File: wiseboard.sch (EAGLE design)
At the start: 87 parts, among them CN1 455-1749-1-ND, CN3 455-1749-1-ND, IC1 MCP73871-2CCI/ML-ND, IC2 LM358MX, Q1 IRLML6402TRPBF, Q2 IRLML6402TRPBF, U1 LT1945EMSPBF, X1 1528-1438-ND

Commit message: ADD ESP DEBUG HEADERS AND ROUGH AUTOROUTE
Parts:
- added ESPDEBUG_1, ESPDEBUG_2: (no value), pinhead:PINHD-1X8
- added INPUTBUTTONHEADER: (no value), pinhead:PINHD-1X2
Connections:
- removed net GPIO2: R24.1
- removed net N$12: JP3.1, X1.GPIO16
- removed net N$17: C8.1, CN1.1, IC1.VBAT1, IC1.VBAT2, IC1.VBAT3, JP2.1
- new net +3V1: ESPDEBUG_1.8
- new net GND1: ESPDEBUG_2.8
- new net GPIO16: ESPDEBUG_1.4, JP3.1, X1.GPIO16
- net +3V3: now also INPUTBUTTONHEADER.1
- net ADC: now also ESPDEBUG_1.2
- net BOOSTENA: now also ESPDEBUG_2.6, R24.1
- net CH_PD: now also ESPDEBUG_1.3
- net CL: now also ESPDEBUG_2.4
- net GPIO0: now also ESPDEBUG_2.5
- net GPIO12: now also ESPDEBUG_1.6; no longer U$13.S
- net GPIO13: now also ESPDEBUG_1.7
- net GPIO14: now also ESPDEBUG_1.5
- net GPIO15: now also ESPDEBUG_2.7
- net N$25: now also U$14.VIN
- net N$26: now also INPUTBUTTONHEADER.2
- net OE: now also ESPDEBUG_2.3
- net RESET: now also ESPDEBUG_1.1
- net RXD: now also ESPDEBUG_2.2, U$13.S
- net TXD: now also ESPDEBUG_2.1
- net VBAT: now also C8.1, CN1.1, IC1.VBAT1, IC1.VBAT2, IC1.VBAT3, JP2.1; no longer U$14.VIN
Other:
- note added: "ESP DEBUG HEADER"
- moved on the sheet: D2

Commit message: PASS ERC SCHEMATIC TEST AND ADD SUPPLY SYMBOLS
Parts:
- removed C13: 1uF, adafruit:C-USC1206
- added INPUTBUTTONHEADER1, SOLARPIN: (no value), pinhead:PINHD-1X2
- C2: value (none) -> 2u2F
- C4: value (none) -> 100pF
- renumbered CN3 to SOLAR
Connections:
- net +20V renamed -20V
- removed net +24V: U$4.GVDD
- removed net +3V1: ESPDEBUG_1.8
- removed net GND1: ESPDEBUG_2.8
- new net +22V: C5.1, R6.2, U$2.VIN, U$4.GVDD, U$8.C
- net +3V3: now also ESPDEBUG_1.8, INPUTBUTTONHEADER1.1
- net ADC: no longer C13.1, U$13.GND
- net GND: now also ESPDEBUG_2.8, SOLARPIN.1, U$13.GND; no longer C13.2
- net GPIO16: now also JP3.2; no longer JP3.1
- net N$26: now also INPUTBUTTONHEADER1.2
- net N$7: now also SOLARPIN.2
- net RESET: now also JP3.1; no longer JP3.2
- net VCC: no longer C5.1, R6.2, U$2.VIN, U$8.C
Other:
- moved on the sheet: JP3

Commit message: RESOLVE CONSISTENCY ISSUES, IGNORE
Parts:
- CN1: value 455-1749-1-ND -> (none)
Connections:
- net GND: now also CN1.1; no longer CN1.2
- net VBAT: now also CN1.2; no longer CN1.1
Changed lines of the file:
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@@
 <layer number="19" name="Unrouted" color="6" fill="1" visible="no" active="no"/>
 <layer number="20" name="Dimension" color="15" fill="1" visible="no" active="no"/>
-<layer number="21" name="tPlace" color="14" fill="1" visible="no" active="no"/>
+<layer number="21" name="tPlace" color="7" fill="1" visible="no" active="no"/>
 <layer number="22" name="bPlace" color="7" fill="1" visible="no" active="no"/>
 <layer number="23" name="tOrigins" color="15" fill="1" visible="no" active="no"/>
@@
 <part name="U$2" library="WISE" deviceset="L78L15" device="" value="497-7278-1-ND"/>
 <part name="U$3" library="WISE" deviceset="L79L15" device="" value="497-7303-1-ND"/>
-<part name="CN1" library="adafruit" deviceset="JST_2PIN" device="-SMT-RA" value="455-1749-1-ND"/>
 <part name="C1" library="adafruit" deviceset="C-US" device="C1206" value="100nF"/>
 <part name="22" library="WISE" deviceset="587-2103-1-ND" device=""/>
@@
 <part name="GND14" library="supply1" library_urn="urn:adsk.eagle:library:371" deviceset="GND" device=""/>
 <part name="GND15" library="supply1" library_urn="urn:adsk.eagle:library:371" deviceset="GND" device=""/>
-<part name="GND16" library="supply1" library_urn="urn:adsk.eagle:library:371" deviceset="GND" device=""/>
 <part name="C8" library="adafruit" deviceset="C-US" device="C1206" value="10uF"/>
 <part name="GND17" library="supply1" library_urn="urn:adsk.eagle:library:371" deviceset="GND" device=""/>
@@
 <part name="U$19" library="WISE" deviceset="-15V" device=""/>
 <part name="GND46" library="supply1" library_urn="urn:adsk.eagle:library:371" deviceset="GND" device=""/>
+<part name="CN1" library="adafruit" deviceset="JST_2PIN" device="-SMT-RA"/>
+<part name="GND16" library="supply1" library_urn="urn:adsk.eagle:library:371" deviceset="GND" device=""/>
 </parts>
 <sheets>
@@
 <instance part="U$2" gate="G$1" x="-144.78" y="-78.74"/>
 <instance part="U$3" gate="G$1" x="-144.78" y="-7.62"/>
-<instance part="CN1" gate="G$1" x="375.92" y="-154.94"/>
 <instance part="C1" gate="G$1" x="-114.3" y="-7.62"/>
 <instance part="22" gate="G$1" x="-261.62" y="-5.08" rot="R90"/>
@@
 <instance part="GND14" gate="1" x="-124.46" y="-20.32" rot="R90"/>
 <instance part="GND15" gate="1" x="304.8" y="-177.8"/>
-<instance part="GND16" gate="1" x="358.14" y="-157.48"/>
 <instance part="C8" gate="G$1" x="353.06" y="-165.1"/>
 <instance part="GND17" gate="1" x="353.06" y="-175.26"/>
@@
 <instance part="U$19" gate="G$1" x="-124.46" y="60.96"/>
 <instance part="GND46" gate="1" x="-363.22" y="58.42" rot="R270"/>
+<instance part="CN1" gate="G$1" x="375.92" y="-154.94"/>
+<instance part="GND16" gate="1" x="360.68" y="-152.4" rot="R270"/>
 </instances>
 <busses>
@@
 </segment>
 <segment>
-<pinref part="CN1" gate="G$1" pin="2"/>
-<pinref part="GND16" gate="1" pin="GND"/>
-<wire x1="373.38" y1="-154.94" x2="358.14" y2="-154.94" width="0.1524" layer="91"/>
-</segment>
-<segment>
 <pinref part="C8" gate="G$1" pin="2"/>
 <pinref part="GND17" gate="1" pin="GND"/>
@@
 <wire x1="-360.68" y1="58.42" x2="-342.9" y2="58.42" width="0.1524" layer="91"/>
 <pinref part="GND46" gate="1" pin="GND"/>
+</segment>
+<segment>
+<pinref part="CN1" gate="G$1" pin="1"/>
+<wire x1="373.38" y1="-152.4" x2="363.22" y2="-152.4" width="0.1524" layer="91"/>
+<pinref part="GND16" gate="1" pin="GND"/>
 </segment>
 </net>
@@
 <junction x="327.66" y="-149.86"/>
 <junction x="327.66" y="-152.4"/>
-<pinref part="CN1" gate="G$1" pin="1"/>
 <wire x1="327.66" y1="-152.4" x2="347.98" y2="-152.4" width="0.1524" layer="91"/>
 <pinref part="C8" gate="G$1" pin="1"/>
 <wire x1="347.98" y1="-152.4" x2="353.06" y2="-152.4" width="0.1524" layer="91"/>
-<wire x1="353.06" y1="-152.4" x2="373.38" y2="-152.4" width="0.1524" layer="91"/>
-<wire x1="353.06" y1="-162.56" x2="353.06" y2="-152.4" width="0.1524" layer="91"/>
-<junction x="353.06" y="-152.4"/>
+<wire x1="353.06" y1="-162.56" x2="353.06" y2="-154.94" width="0.1524" layer="91"/>
+<wire x1="353.06" y1="-154.94" x2="353.06" y2="-152.4" width="0.1524" layer="91"/>
 <wire x1="347.98" y1="-152.4" x2="347.98" y2="-137.16" width="0.1524" layer="91"/>
 <wire x1="347.98" y1="-137.16" x2="373.38" y2="-137.16" width="0.1524" layer="91"/>
@@
 <pinref part="U$18" gate="G$1" pin="VBAT"/>
 <junction x="347.98" y="-137.16"/>
-</segment>
-</net>
+<pinref part="CN1" gate="G$1" pin="2"/>
+<wire x1="373.38" y1="-154.94" x2="353.06" y2="-154.94" width="0.1524" layer="91"/>
+<junction x="353.06" y="-154.94"/>
+</segment>
+</net>

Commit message: CONTINUED MODIFYING SOLAR CHARGER
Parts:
- removed C10: 4700uF/10V, adafruit:CPOL-USE5-13
- added DONE1: GREEN, adafruit:LEDCHIP-LED0805
- added U2: BQ24210DQCT, WISE:BQ24210DQCT
- C9: value 10uF/10V -> 2u2F; device adafruit:C-USC0805K -> adafruit:C-USC1206
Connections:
- net GND: now also DONE.C, U2.EPAD, U2.VSS; no longer C10.-
- net N$10: now also CHRG/LBO.C, R14.1; no longer IC1./PG, PWR.C
- net N$11: now also PWR.A, R12.2; no longer DONE.C, IC1.STAT2
- net N$13: now also C9.1, D1.C, U2.VBUS; no longer CHRG/LBO.A, R12.1
- net N$15: now also R13.2, R14.2, U2.!CHG; no longer PWR.A, R14.1
- net N$16: now also DONE1.C, U2.!PG; no longer CHRG/LBO.C, IC1.STAT1/LBO
- net VBAT: now also CHRG/LBO.A, DONE1.A, U2.BAT; no longer IC1.VBAT1, IC1.VBAT2, IC1.VBAT3
- net VCC: no longer C10.+, C9.1, D1.C, R12.2, R13.2, R14.2
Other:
- note added: "Programing Header"
- note removed: "Program Header"
- moved on the sheet: C8, C9, CHRG/LBO, CN1, D1, DONE, JP2, PWR, R12, R13, R14, SOLAR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

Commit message: WORK ON NEW CHARGER
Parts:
- added R36, R37: 790, adafruit:R-US_R1206
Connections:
- new net N$17: R36.2, U2.ISET
- new net N$28: R37.2, U2.TS
- net GND: now also R36.1, R37.1
- net N$16: now also U2.!EN
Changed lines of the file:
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@@
 <part name="U$22" library="WISE" deviceset="VBAT" device=""/>
 <part name="GND21" library="supply1" library_urn="urn:adsk.eagle:library:371" deviceset="GND" device=""/>
+<part name="R36" library="adafruit" deviceset="R-US_" device="R1206" value="790"/>
+<part name="GND49" library="supply1" library_urn="urn:adsk.eagle:library:371" deviceset="GND" device=""/>
+<part name="R37" library="adafruit" deviceset="R-US_" device="R1206" value="790"/>
+<part name="GND50" library="supply1" library_urn="urn:adsk.eagle:library:371" deviceset="GND" device=""/>
 </parts>
 <sheets>
@@
 <instance part="GND16" gate="1" x="500.38" y="-200.66" rot="R270"/>
 <instance part="U2" gate="A" x="482.6" y="-129.54"/>
-<instance part="GND47" gate="1" x="467.36" y="-134.62" rot="R270"/>
+<instance part="GND47" gate="1" x="462.28" y="-162.56"/>
 <instance part="U$20" gate="G$1" x="558.8" y="-132.08" rot="R270"/>
 <instance part="GND48" gate="1" x="589.28" y="-165.1"/>
@@
 <instance part="U$22" gate="G$1" x="574.04" y="-165.1" rot="R180"/>
 <instance part="GND21" gate="1" x="551.18" y="-129.54" rot="R90"/>
+<instance part="R36" gate="G$1" x="462.28" y="-137.16" rot="R90"/>
+<instance part="GND49" gate="1" x="469.9" y="-134.62" rot="R270"/>
+<instance part="R37" gate="G$1" x="477.52" y="-152.4" rot="R90"/>
+<instance part="GND50" gate="1" x="477.52" y="-162.56"/>
 </instances>
 <busses>
@@
 </segment>
 <segment>
-<pinref part="U2" gate="A" pin="VSS"/>
-<wire x1="485.14" y1="-134.62" x2="469.9" y2="-134.62" width="0.1524" layer="91"/>
-<pinref part="GND47" gate="1" pin="GND"/>
-</segment>
-<segment>
 <pinref part="DONE" gate="G$1" pin="C"/>
 <pinref part="GND48" gate="1" pin="GND"/>
@@
 <pinref part="GND21" gate="1" pin="GND"/>
 <wire x1="548.64" y1="-129.54" x2="541.02" y2="-129.54" width="0.1524" layer="91"/>
+</segment>
+<segment>
+<pinref part="GND47" gate="1" pin="GND"/>
+<pinref part="R36" gate="G$1" pin="1"/>
+<wire x1="462.28" y1="-160.02" x2="462.28" y2="-142.24" width="0.1524" layer="91"/>
+</segment>
+<segment>
+<pinref part="U2" gate="A" pin="VSS"/>
+<pinref part="GND49" gate="1" pin="GND"/>
+<wire x1="472.44" y1="-134.62" x2="485.14" y2="-134.62" width="0.1524" layer="91"/>
+</segment>
+<segment>
+<pinref part="R37" gate="G$1" pin="1"/>
+<pinref part="GND50" gate="1" pin="GND"/>
+<wire x1="477.52" y1="-160.02" x2="477.52" y2="-157.48" width="0.1524" layer="91"/>
 </segment>
 </net>
@@
 <pinref part="DONE1" gate="G$1" pin="C"/>
 <wire x1="546.1" y1="-142.24" x2="546.1" y2="-152.4" width="0.1524" layer="91"/>
-</segment>
-</net>
+<pinref part="U2" gate="A" pin="!EN"/>
+<wire x1="541.02" y1="-139.7" x2="546.1" y2="-139.7" width="0.1524" layer="91"/>
+<wire x1="546.1" y1="-139.7" x2="546.1" y2="-142.24" width="0.1524" layer="91"/>
+<junction x="546.1" y="-142.24"/>
+</segment>
+</net>
+<net name="N$17" class="0">
+<segment>
+<pinref part="U2" gate="A" pin="ISET"/>
+<pinref part="R36" gate="G$1" pin="2"/>
+<wire x1="462.28" y1="-132.08" x2="485.14" y2="-132.08" width="0.1524" layer="91"/>
+</segment>
+</net>
+<net name="N$28" class="0">
+<segment>
+<pinref part="U2" gate="A" pin="TS"/>
+<pinref part="R37" gate="G$1" pin="2"/>
+<wire x1="485.14" y1="-139.7" x2="477.52" y2="-139.7" width="0.1524" layer="91"/>
+<wire x1="477.52" y1="-139.7" x2="477.52" y2="-147.32" width="0.1524" layer="91"/>
+</segment>
+</net>

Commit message: SEMI-FINALIZE NEW CHARGER IC
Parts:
- removed DONE1: GREEN, adafruit:LEDCHIP-LED0805
- removed IC1: MCP73871-2CCI/ML-ND, adafruit:MCP73871
- removed PWR: RED, adafruit:LEDCHIP-LED0805
- removed R11: 100K, adafruit:R-US_M1206
- removed R12: 1K, adafruit:R-US_M1206
- removed R15: 1K, adafruit:R-US_R1206
- removed R16: 150K, adafruit:R-US_R1206
- removed R17: 10K, adafruit:R-US_R1206
- removed R18: 2K, adafruit:R-US_R1206
- removed R19: 100K, adafruit:R-US_R1206
- added JP4: JUMPER, Sparkfun-Passives:JUMPER-SMT_2_NC_PASTE_NO-SILK
- added POWERGOOD: BLUE, adafruit:LEDCHIP-LED0805
- added R38: 7.6k, adafruit:R-US_R1206
- R10: value 270K -> 1K
- R37: value 790 -> 10k
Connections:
- removed net N$16: DONE1.C, U2.!EN, U2.!PG
- removed net N$18: IC1.THERM, R15.2
- removed net N$19: R15.1, R16.1, R17.1
- removed net N$20: IC1.PROG1, R18.2
- removed net N$21: IC1.PROG3, R19.2
- new net CHARGE_EN: JP4.2, U$12.QP3, U2.!EN
- new net N$30: R38.2, U2.VTSB
- net GND: now also JP4.1; no longer IC1.GND1, IC1.GND2, R11.1, R16.2, R17.2, R18.1, R19.1
- net N$11: now also POWERGOOD.C, R10.1; no longer PWR.A, R12.2
- net N$28: now also R38.1
- net N$9: now also R10.2, U2.!PG; no longer IC1.VPCC, R10.1, R11.2
- net VBAT: now also POWERGOOD.A; no longer DONE1.A
- net VCC: no longer IC1./TE, IC1.CE, IC1.IN1, IC1.IN2, IC1.PROG2, IC1.SEL, R10.2
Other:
- moved on the sheet: C8, C9, CHRG/LBO, CN1, D1, DONE, JP2, R10, R13, R14, R36, R37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

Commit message: ROUTE REV 1.5 BOARD
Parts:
- removed INPUTBUTTONHEADER1: (no value), pinhead:PINHD-1X2
- removed R26: 4K7, adafruit:R-US_M1206
- removed R27: 10K, adafruit:R-US_M1206
- renumbered CN1 to BAT_CON, JP2 to BAT_PIN
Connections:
- removed net N$25: D2.C, R22.1, U$14.VIN
- new net N$16: C11.1, U$11.OE, U$11.VCC
- net +3V3: no longer INPUTBUTTONHEADER1.1
- net ADC: no longer R26.1, R27.2
- net GND: no longer R27.1
- net N$26: no longer INPUTBUTTONHEADER1.2
- net VCC: now also D2.C, R22.1, U$14.VIN
- net VDD: no longer C11.1, R26.2, U$11.OE, U$11.VCC
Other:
- note removed: "Solar Panel Connector"

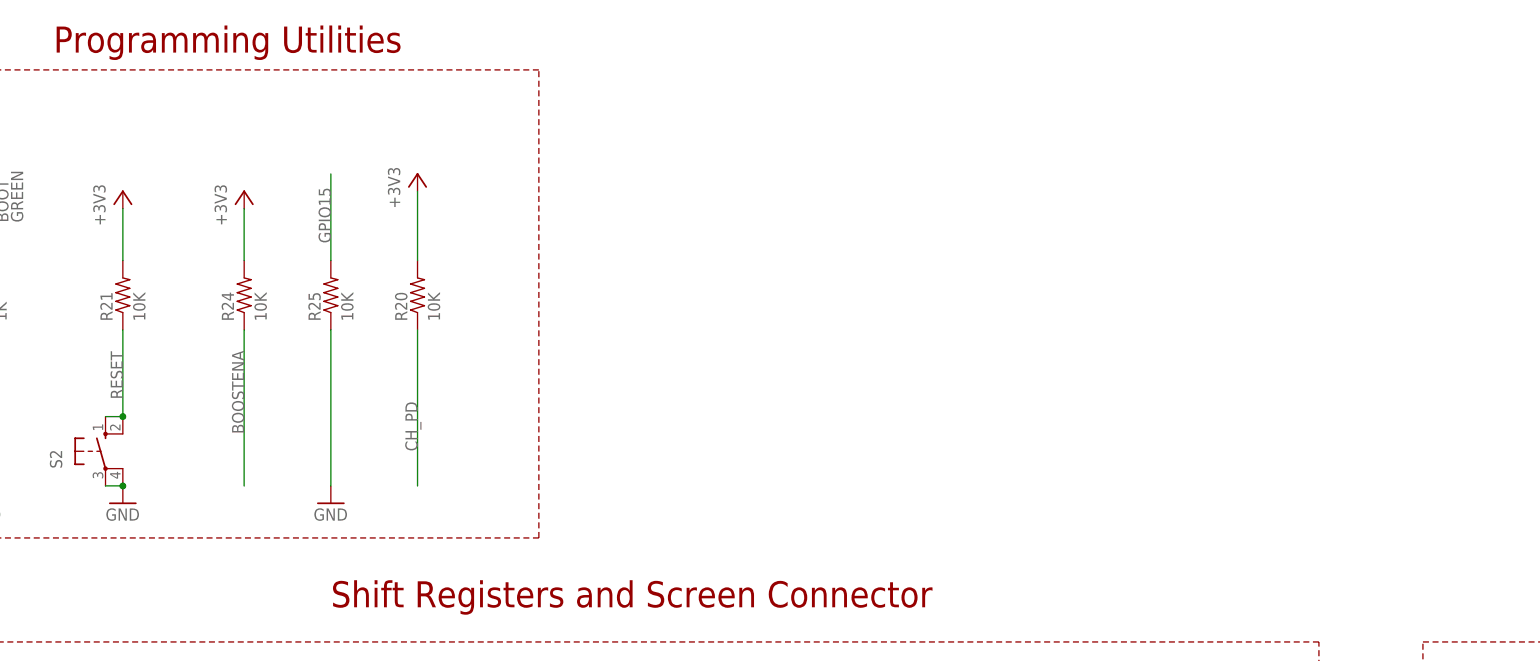
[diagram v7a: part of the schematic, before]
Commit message: ADD W25Q32JV FLASH CHIP TO SCHEMATIC
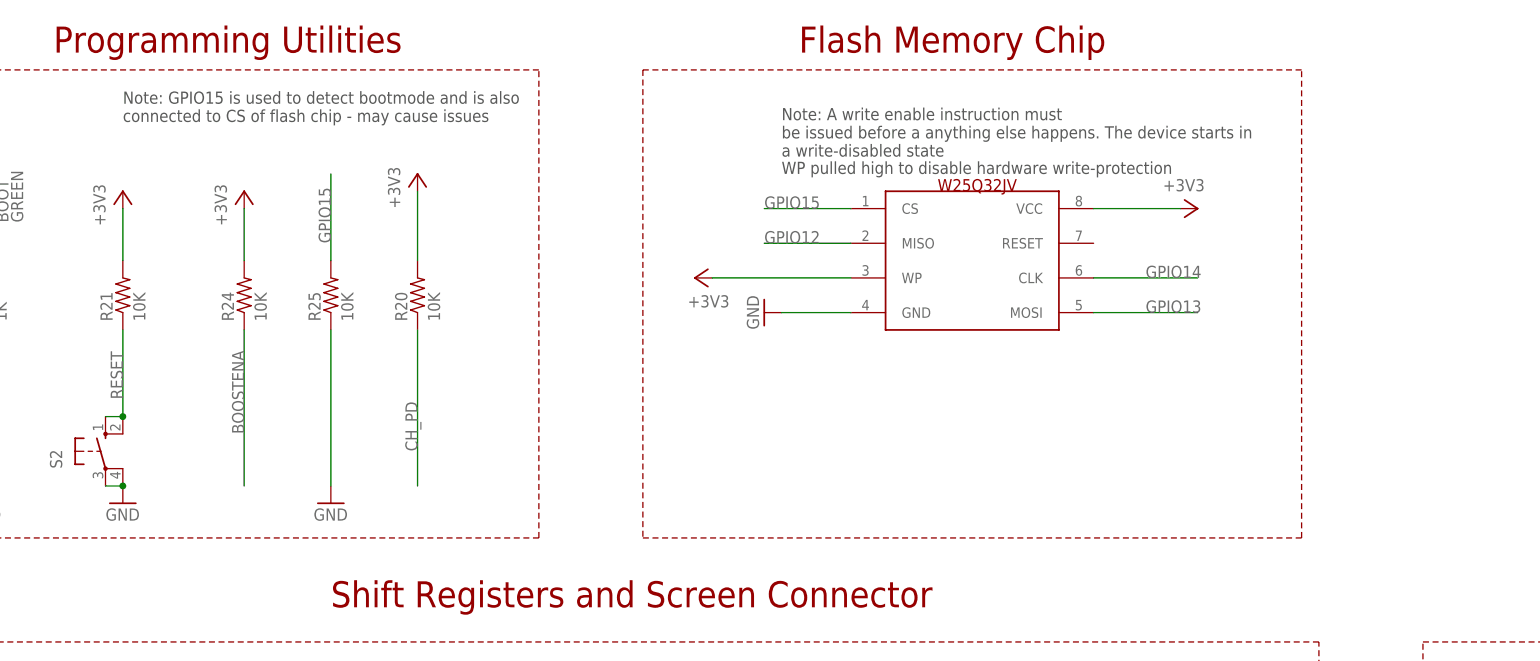
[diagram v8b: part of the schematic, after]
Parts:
- added U$23: W25Q32JVSSIQ, WISE:W25Q32JVSSIQ
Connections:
- net +3V3: now also U$23.VCC, U$23.WP
- net GND: now also U$23.GND
- net GPIO12: now also U$23.MISO
- net GPIO13: now also U$23.MOSI
- net GPIO14: now also U$23.CLK
- net GPIO15: now also U$23.CS
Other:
- note added: "Flash Memory Chip"
- note added: "Note: A write enable instruction must be issued before a anything else happens. The device starts in a write-disabled state"
- note added: "Note: GPIO15 is used to detect bootmode and is also connected to CS of flash chip - may cause issues"
- note added: "WP pulled high to disable hardware write-protection"
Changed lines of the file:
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@@
 <part name="GND15" library="supply1" library_urn="urn:adsk.eagle:library:371" deviceset="GND" device=""/>
 <part name="P+2" library="supply1" library_urn="urn:adsk.eagle:library:371" deviceset="VCC" device=""/>
+<part name="U$23" library="WISE" deviceset="W25Q32JVSSIQ" device=""/>
+<part name="GND20" library="supply1" library_urn="urn:adsk.eagle:library:371" deviceset="GND" device=""/>
+<part name="+3V13" library="supply1" library_urn="urn:adsk.eagle:library:371" deviceset="+3V3" device=""/>
+<part name="+3V14" library="supply1" library_urn="urn:adsk.eagle:library:371" deviceset="+3V3" device=""/>
 </parts>
 <sheets>
@@
 <wire x1="391.16" y1="-66.04" x2="391.16" y2="22.86" width="0.1524" layer="94" style="shortdash"/>
 <text x="406.4" y="27.94" size="2.54" layer="94">ESP DEBUG HEADER</text>
+<text x="20.32" y="104.14" size="1.778" layer="97">Note: GPIO15 is used to detect bootmode and is also
+connected to CS of flash chip - may cause issues</text>
+<text x="116.84" y="99.06" size="1.778" layer="97">Note: A write enable instruction must
+be issued before a anything else happens. The device starts in
+a write-disabled state</text>
+<text x="116.84" y="96.52" size="1.778" layer="97">WP pulled high to disable hardware write-protection</text>
+<wire x1="96.52" y1="111.76" x2="96.52" y2="43.18" width="0.1524" layer="94" style="shortdash"/>
+<wire x1="96.52" y1="43.18" x2="193.04" y2="43.18" width="0.1524" layer="94" style="shortdash"/>
+<wire x1="193.04" y1="43.18" x2="193.04" y2="111.76" width="0.1524" layer="94" style="shortdash"/>
+<wire x1="193.04" y1="111.76" x2="96.52" y2="111.76" width="0.1524" layer="94" style="shortdash"/>
+<text x="119.38" y="114.3" size="3.81" layer="94">Flash Memory Chip</text>
 </plain>
 <instances>
@@
 <instance part="GND15" gate="1" x="365.76" y="-142.24"/>
 <instance part="P+2" gate="VCC" x="360.68" y="106.68"/>
+<instance part="U$23" gate="G$1" x="144.78" y="83.82"/>
+<instance part="GND20" gate="1" x="114.3" y="76.2" rot="R270"/>
+<instance part="+3V13" gate="G$1" x="177.8" y="91.44" rot="R270"/>
+<instance part="+3V14" gate="G$1" x="104.14" y="81.28" rot="R90"/>
 </instances>
 <busses>
@@
 <wire x1="365.76" y1="-132.08" x2="365.76" y2="-139.7" width="0.1524" layer="91"/>
 <pinref part="GND15" gate="1" pin="GND"/>
+</segment>
+<segment>
+<pinref part="U$23" gate="G$1" pin="GND"/>
+<wire x1="127" y1="76.2" x2="116.84" y2="76.2" width="0.1524" layer="91"/>
+<pinref part="GND20" gate="1" pin="GND"/>
 </segment>
 </net>
@@
 <pinref part="ESPDEBUG_1" gate="A" pin="6"/>
 </segment>
+<segment>
+<pinref part="U$23" gate="G$1" pin="MISO"/>
+<wire x1="127" y1="86.36" x2="114.3" y2="86.36" width="0.1524" layer="91"/>
+<label x="114.3" y="86.36" size="1.778" layer="95"/>
+</segment>
 </net>
 <net name="GPIO14" class="0">
@@
 <pinref part="ESPDEBUG_1" gate="A" pin="5"/>
 </segment>
+<segment>
+<pinref part="U$23" gate="G$1" pin="CLK"/>
+<wire x1="162.56" y1="81.28" x2="177.8" y2="81.28" width="0.1524" layer="91"/>
+<label x="170.18" y="81.28" size="1.778" layer="95"/>
+</segment>
 </net>
 <net name="GPIO13" class="0">
@@
 <label x="401.32" y="-33.02" size="1.778" layer="95"/>
 <pinref part="ESPDEBUG_1" gate="A" pin="7"/>
+</segment>
+<segment>
+<pinref part="U$23" gate="G$1" pin="MOSI"/>
+<wire x1="162.56" y1="76.2" x2="177.8" y2="76.2" width="0.1524" layer="91"/>
+<label x="170.18" y="76.2" size="1.778" layer="95"/>
 </segment>
 </net>
@@
 <pinref part="+3V12" gate="G$1" pin="+3V3"/>
 </segment>
+<segment>
+<pinref part="U$23" gate="G$1" pin="VCC"/>
+<wire x1="162.56" y1="91.44" x2="175.26" y2="91.44" width="0.1524" layer="91"/>
+<pinref part="+3V13" gate="G$1" pin="+3V3"/>
+</segment>
+<segment>
+<pinref part="U$23" gate="G$1" pin="WP"/>
+<wire x1="127" y1="81.28" x2="106.68" y2="81.28" width="0.1524" layer="91"/>
+<pinref part="+3V14" gate="G$1" pin="+3V3"/>
+</segment>
 </net>
 <net name="RXD" class="0">
@@
 <pinref part="ESPDEBUG_2" gate="A" pin="7"/>
 </segment>
-</net>
+<segment>
+<pinref part="U$23" gate="G$1" pin="CS"/>
+<wire x1="127" y1="91.44" x2="114.3" y2="91.44" width="0.1524" layer="91"/>
+<label x="114.3" y="91.44" size="1.778" layer="95"/>
+</segment>
+</net>
